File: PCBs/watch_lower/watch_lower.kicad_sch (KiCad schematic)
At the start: 17 parts, among them J1 AXG220144, U1 MAX30102EFD+T, U2 DRV2605LYZFR

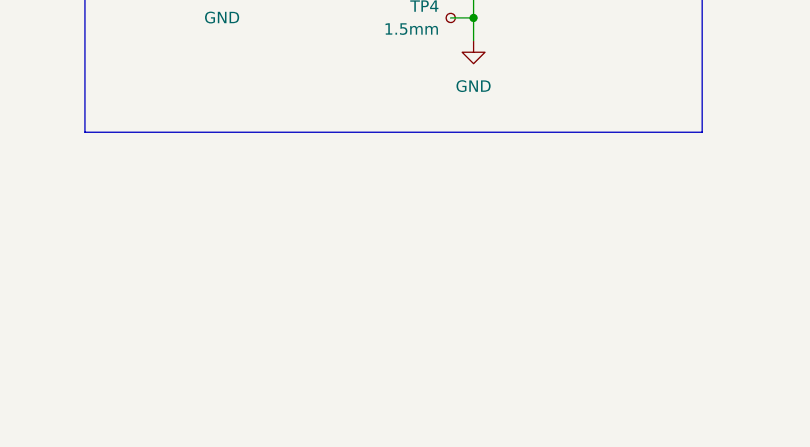
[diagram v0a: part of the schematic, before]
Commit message: RFID PCB Done, started lower flex PCB
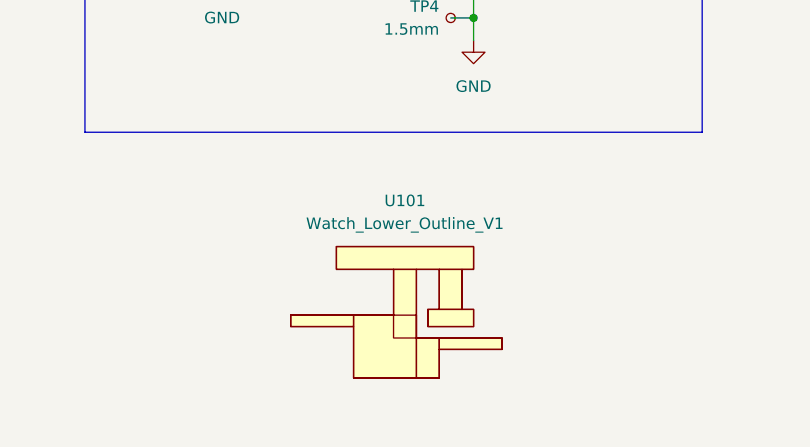
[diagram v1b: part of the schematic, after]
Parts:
- added U101: Watch_Lower_Outline_V1, watch_footprints:Watch Lower Outline V1, symbol watch_symbols_lib:Watch_Lower_Outline_V1_1
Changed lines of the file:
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@@
+    )
+  )
+  (symbol (lib_id "watch_symbols_lib:Watch_Lower_Outline_V1_1") (at 132.08 167.64 0) (unit 1)
+    (in_bom no) (on_board yes) (dnp no)
+    (property "Reference" "U101" (at 132.08 154.94 0)
+      (effects (font (size 1.27 1.27)))
+    )
+    (property "Value" "Watch_Lower_Outline_V1" (at 132.08 157.48 0)
+      (effects (font (size 1.27 1.27)))
+    )
+    (property "Footprint" "watch_footprints:Watch Lower Outline V1" (at 132.08 177.8 0)
+      (effects (font (size 1.27 1.27)) hide)
+    )
+    (property "Datasheet" "" (at 132.08 162.56 0)
+      (effects (font (size 1.27 1.27)) hide)
+    )
+    (instances
+      (project "watch_lower"
+        (path "/45c8db28-ef4f-4950-9b2b-4b58c2d8cdd0"
+          (reference "U101") (unit 1)
+        )
+      )
     )
   )

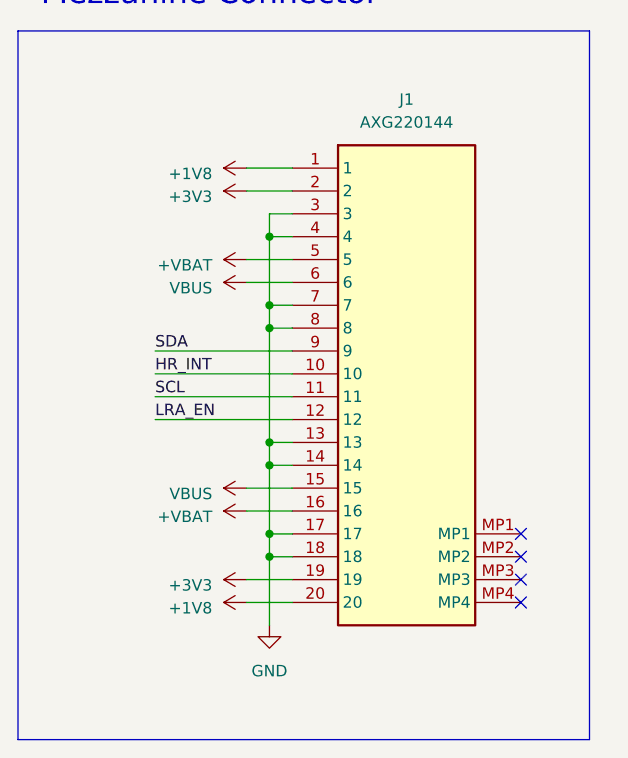
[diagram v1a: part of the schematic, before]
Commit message: Flex PCB finished. Need to rotate RFID transponder coil.
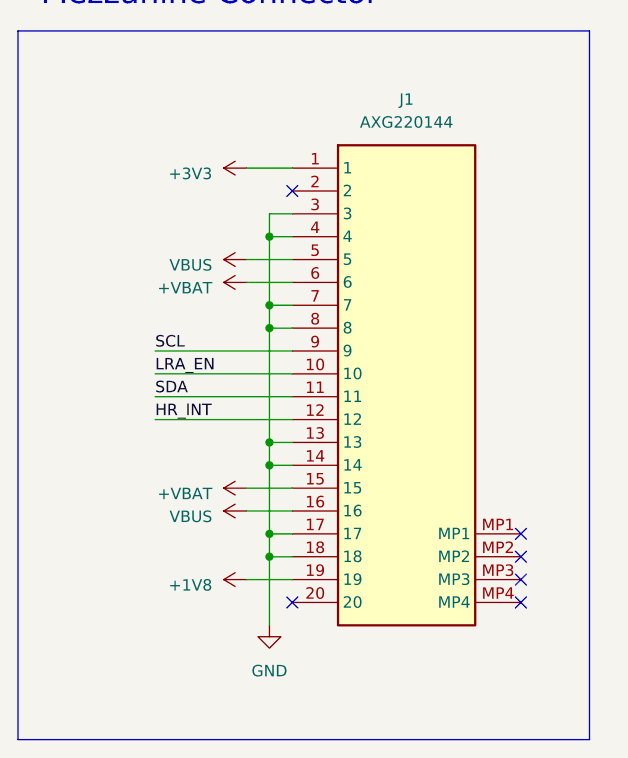
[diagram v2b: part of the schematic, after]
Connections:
- net +1V8: now also J1.19; no longer J1.1, J1.20
- net +3V3: now also J1.1; no longer J1.19, J1.2
- net +VBAT: now also J1.15, J1.6; no longer J1.16, J1.5
- net HR_INT: now also J1.12; no longer J1.10
- net LRA_EN: now also J1.10; no longer J1.12
- net SCL: now also J1.9; no longer J1.11
- net SDA: now also J1.11; no longer J1.9
- net VBUS: now also J1.16, J1.5; no longer J1.15, J1.6
- no-connect marks 10 -> 12

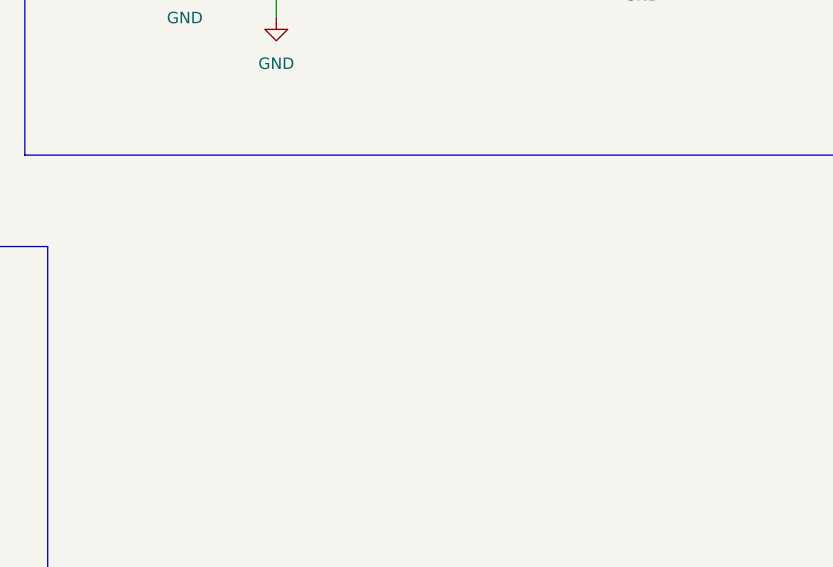
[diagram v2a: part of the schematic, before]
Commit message: Added comments to RFID module and created gerber files.
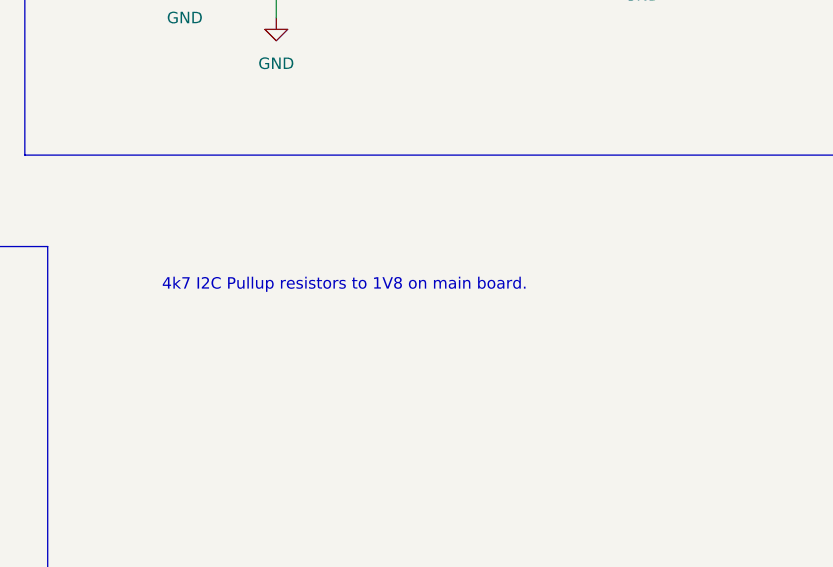
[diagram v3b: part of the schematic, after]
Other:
- note added: "4k7 I2C Pullup resistors to 1V8 on main board."
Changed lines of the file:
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@@
     (effects (font (size 2.54 2.54)) (justify left bottom))
+  )
+  (text "4k7 I2C Pullup resistors to 1V8 on main board." (at 177.8 106.68 0)
+    (effects (font (size 1.27 1.27)) (justify left bottom))
   )
   (label "HR_INT" (at 33.02 58.42 0) (fields_autoplaced)

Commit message: Started watch_main_v3
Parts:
- added C101, C102: C_Small, symbol Device:C_Small
- added J101, J102, J103, J105: Digital Input, symbol Connector_Generic:Conn_01x01
- added R101, R102, R103, R104: R_Small, symbol Device:R_Small
- added SW101, SW102, SW103, SW105: SW_SPST, symbol Switch:SW_SPST
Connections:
- net +3V3: now also R101.1, R102.1, R103.1
- net GND: now also C101.2, C102.2, SW101.1 (A), SW102.1 (A), SW103.1 (A), SW105.1 (A)
- new net: C101.1, J105.1 (Pin_1), R102.2, SW105.2 (B)
- new net: R104.1, SW103.2 (B)
- new net: C102.1, J103.1 (Pin_1), R103.2, R104.2
- new net: J101.1 (Pin_1), SW101.2 (B)
- new net: J102.1 (Pin_1), R101.2, SW102.2 (B)
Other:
- note added: "Button"
- note added: "Debouncing Capacitor"
- note added: "Digital Input"
- note added: "Pull-up Resistor"
